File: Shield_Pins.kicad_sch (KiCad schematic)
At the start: 0 parts

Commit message: 1st push attempt
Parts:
- added AE1: Antenna, symbol Device:Antenna
- added BT1: Battery_Cell, symbol Device:Battery_Cell
- added C? (x5): C, symbol Device:C
- added L?: INDUCTOR, symbol pspice:INDUCTOR
- added P?: USB_C_Plug_USB2.0, symbol Connector:USB_C_Plug_USB2.0
- added Q?: BF244A, Package_TO_SOT_THT:TO-92_Inline, symbol Transistor_FET:BF244A
- added SW1, SW2: SW_DIP_x01, symbol Switch:SW_DIP_x01
- added U1: NEO-M8Q, RF_GPS:ublox_NEO, symbol RF_GPS:NEO-M8Q
- added U? (x2): AP2127N-3.3, Package_TO_SOT_SMD:SOT-23, symbol Regulator_Linear:AP2127N-3.3
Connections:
- new net: AE1.1 (A), C?.1, L?.1
- new net: C?.1, L?.2, SW2.1
- new net: P?.A4 (VBUS), P?.A9 (VBUS), P?.B4 (VBUS), P?.B9 (VBUS), U?.3 (VI)
- new net: BT1.2 (-), C?.2
- new net +5V: U?.3 (VI)
- new net ANT: SW2.2, U1.11 (RF_IN)
- new net BATT_3.3: BT1.1 (+), C?.1, U1.22 (V_BCKP)
- new net D_MINUS: P?.A7 (D-), U1.5 (USB_DM)
- new net D_PLUS: P?.A6 (D+), U1.6 (USB_DP)
- new net EXT_ANT_EN: U1.14 (LNA_EN)
- new net EXT_ANT_PWR: U1.9 (VCC_RF)
- new net GND: C?.2, C?.2, C?.2, C?.2, P?.A1 (GND), P?.A12 (GND), P?.B1 (GND), P?.B12 (GND), Q?.3 (S), SW1.2, U1.10 (GND), U1.12 (GND), U1.13 (GND), U1.24 (GND), U?.1 (GND), U?.1 (GND)
- new net IO.11: U1.18 (SDA/~{SPI_CS})
- new net IO.12: U1.19 (SCL/SPI_CLK)
- new net IO.7: U1.4 (EXTINT)
- new net IO.8: Q?.2 (G)
- new net IO.RX: U1.21 (RXD/SPI_MOSI)
- new net IO.SDO: U1.20 (TXD/SPI_MISO)
- new net MAIN_3.3: C?.1, U1.23 (VCC), U?.2 (VO)
- new net SERVICE: U1.1 (~{SAFEBOOT})
- new net SPI_SEL: Q?.1 (D), SW1.1, U1.2 (D_SEL)
- new net USB_3.3: C?.1, U1.7 (VDD_USB), U?.2 (VO)
- no-connect marks 5 -> 1
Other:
- note added: "Battery USB USB 5V to 3.3V 5V to 3.3V Timepulse Attatchment D_SEL Switches Reset Buttons"
- note added: "NEO-M8Q-01A"

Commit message: Schematics V1 done, still need Pi filter numbers
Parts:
- removed C?: C, symbol Device:C
- removed Q?: BF244A, Package_TO_SOT_THT:TO-92_Inline, symbol Transistor_FET:BF244A
- added C1, C5, C7: 0.1 µF, symbol Device:C
- added D1, D2, D3: LED, symbol Device:LED
- added J1, J3, J4: Conn_01x01_Male, symbol Connector:Conn_01x01_Male
- added J2: Conn_01x02_Male, symbol Connector:Conn_01x02_Male
- added R1, R2, R3: 10k, symbol Device:R
- added R4, R5: 330, symbol Device:R
- added R6: 150, symbol Device:R
- added SW1: SW_Push, symbol Switch:SW_Push
- added U1: TXB0108DQSR, Package_SON:USON-20_2x4mm_P0.4mm, symbol Logic_LevelTranslator:TXB0108DQSR
- added U1: 74LS157, symbol 74xx:74LS157
- C2, C6: renamed from C?; value C -> 0.1 µF
- gave numbers to parts that had none: 6
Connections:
- net SPI_SEL is gone; now on net +3V3: SW1.1, U1.2 (D_SEL)
- net +5V: now also C1.1, R4.1, U1.16 (VCCB)
- net ANT: now also J3.1 (Pin_1)
- net EXT_ANT_EN: now also J2.2 (Pin_2)
- net EXT_ANT_PWR: now also J2.1 (Pin_1)
- net GND: now also BT1.2 (-), C1.2, C5.2, C7.2, D1.1 (K), D2.1 (K), D3.1 (K), R1.2, R2.1, R3.1, U1.15 (GND), U1.8 (GND); no longer SW1.2
- net IO.11: now also U1.10 (I1c); no longer U1.18 (SDA/~{SPI_CS})
- net IO.12: now also U1.13 (I1d); no longer U1.19 (SCL/SPI_CLK)
- net IO.8: now also U1.20 (B1)
- net IO.RX: now also U1.6 (I1b); no longer U1.21 (RXD/SPI_MOSI)
- net IO.SDO: now also U1.2 (I0a); no longer U1.20 (TXD/SPI_MISO)
- net SERVICE: now also J1.1 (Pin_1)
- net USB_5V: now reaches P1.A4 (VBUS), P1.A9 (VBUS), P1.B4 (VBUS), P1.B9 (VBUS), U2.3 (VI)
- net USB_5V: now also C5.1, R5.1
- net at P1.A5 (CC): now also R2.2
- net at P1.B5 (VCONN): now also R1.1
- net PULSE_3.3: now reaches U1.3 (TIMEPULSE)
- net PULSE_3.3: now also R6.1, U1.3 (A3)
- net RESET: now reaches U1.8 (~{RESET})
- net RESET: now also C7.1, SW1.2, U1.2 (A2)
- net BATT_3.3 renamed BATT_3V
- net IO.7 renamed EXT_INT
- net EXT_INT: now also J4.1 (Pin_1), U1.1 (A1)
- net MAIN_3.3 renamed +3V3
- net +3V3: now also SW1.1, U1.1 (S), U1.16 (VCC), U1.5 (VCCA), U1.6 (OE)
- new net: D3.2 (A), R5.2
- new net: D2.2 (A), R4.2
- new net: R3.2, SW1.2
- new net: D1.2 (A), R6.2
- new net IO.10: U1.18 (B3)
- new net IO.9: U1.19 (B2)
- new net IO.CSB: U1.11 (I0c)
- new net IO.SCK: U1.5 (I0b)
- new net IO.SDI: U1.14 (I0d)
- new net IO.TX: U1.3 (I1a)
- new net RX_3.3: U1.21 (RXD/SPI_MOSI), U1.7 (A5)
- new net RX_SCK: U1.14 (B5), U1.7 (Zb)
- new net SCL_3.3: U1.18 (SDA/~{SPI_CS}), U1.19 (SCL/SPI_CLK), U1.8 (A6), U1.9 (A7)
- new net SCL_CLK: U1.12 (B7), U1.12 (Zd)
- new net SDA_CSB: U1.13 (B6), U1.9 (Zc)
- new net TX_3.3: U1.20 (TXD/SPI_MISO), U1.4 (A4)
- new net TX_SDO: U1.17 (B4), U1.4 (Za)
- no-connect marks 1 -> 5
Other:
- note added: "2 to 1 Multiplexer"
- note added: "5V to 3.3V LLC - Bidirectional"
- note added: "Additional Pins"
- note added: "Backup Battery"
- note added: "Main Board 5V to 3.3V"
- note added: "Passive Antenna with Switch - Internal"
- note added: "Power and Status LEDs"
- note added: "Reset Circuit"
- note added: "UART/I2C or SPI Switch"
- note added: "USB 5V to 3.3V"
- note added: "USB C Connection"
- note removed: "Battery USB USB 5V to 3.3V 5V to 3.3V Timepulse Attatchment D_SEL Switches Reset Buttons"
- moved on the sheet: AE1, BT1, C2, C3, C4, C6, L1, P1, SW1, SW2, U1, U2

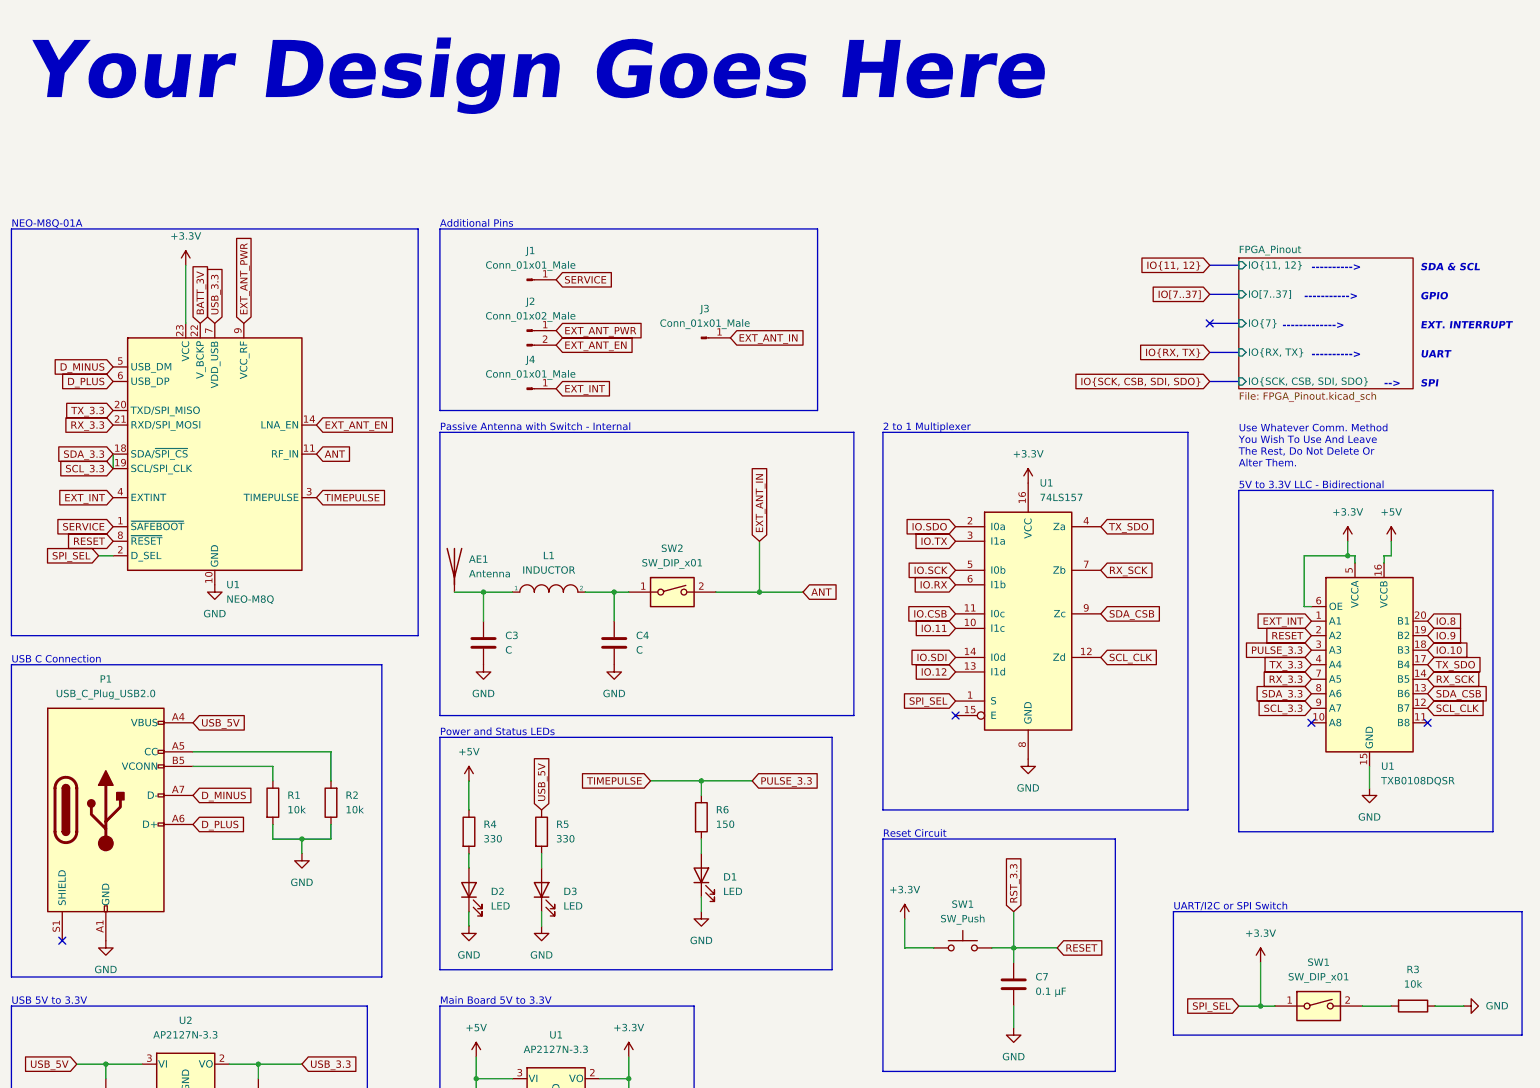
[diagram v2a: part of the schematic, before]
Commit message: Filter values added
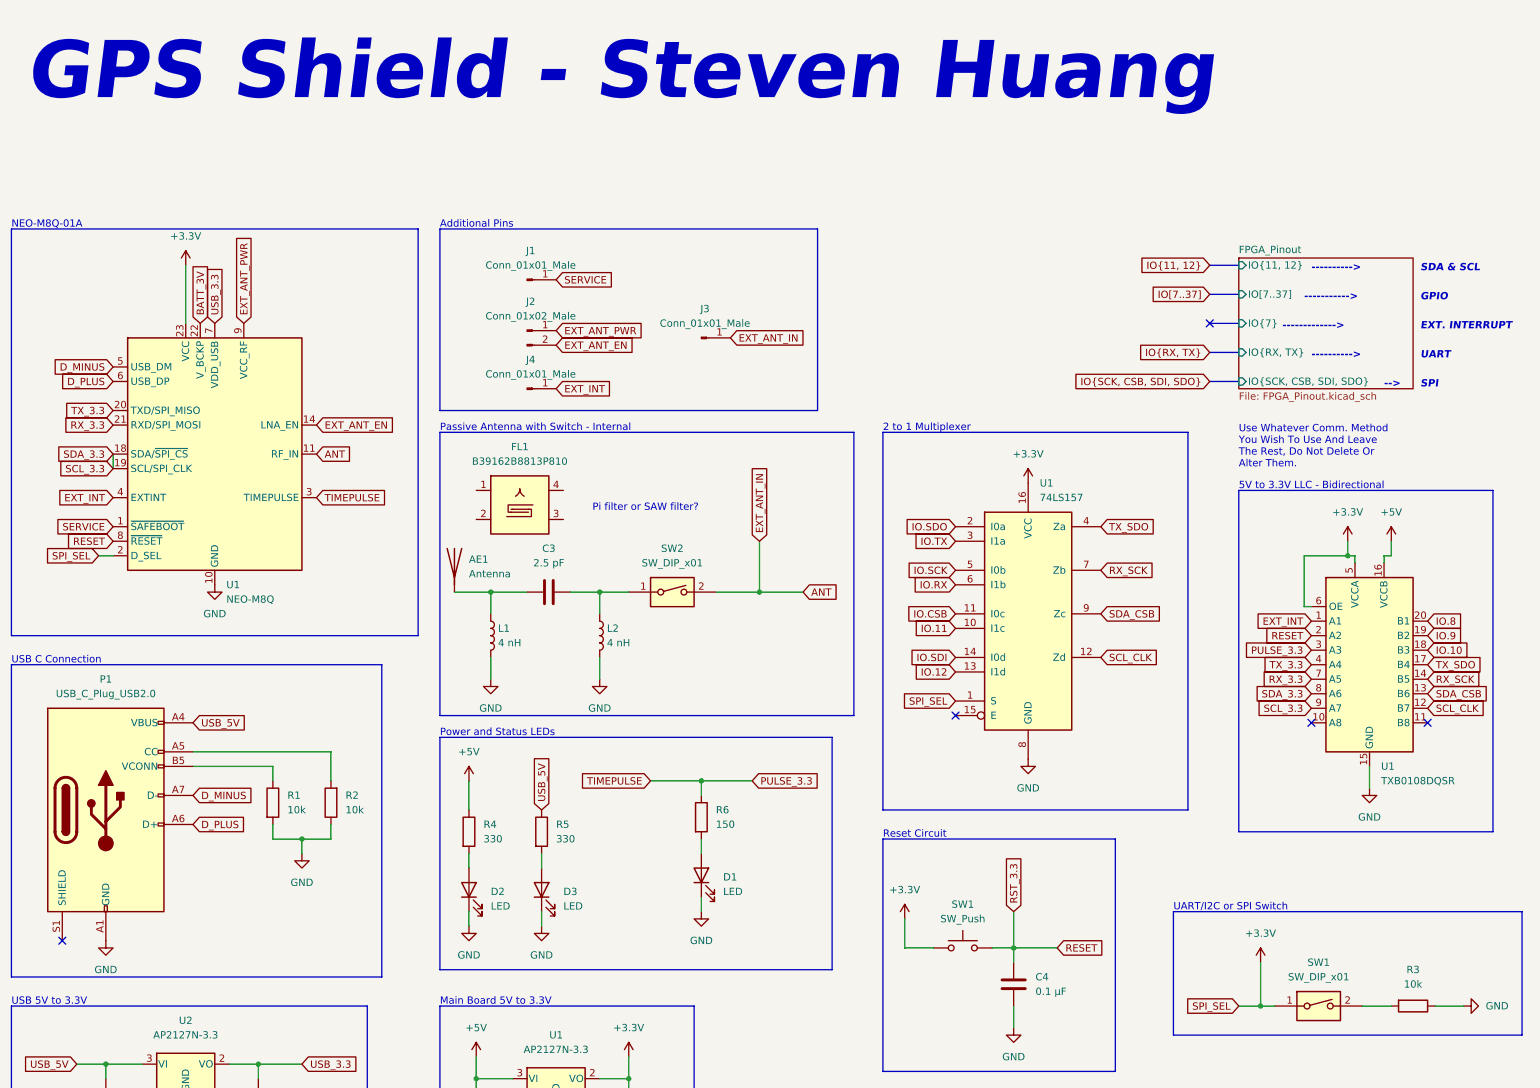
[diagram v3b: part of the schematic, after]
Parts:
- removed C4: C, symbol Device:C
- removed L1: INDUCTOR, symbol pspice:INDUCTOR
- added FL1: B39162B8813P810, Filter:Filter_1109-5_1.1x0.9mm, symbol Filter:B39162B8813P810
- added L1, L2: 4 nH, symbol Device:L
- C3: value C -> 2.5 pF
- renumbered C7 to C4
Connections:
- net GND: now also L1.2, L2.2; no longer C3.2
- net at AE1.1 (A), C3.1: now also L1.1
- net at SW2.1: now also C3.2, L2.1
- new net: FL1.2, FL1.5
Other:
- note added: "GPS Shield - Steven Huang"
- note added: "Pi filter or SAW filter?"
- note removed: "Your Design Goes Here"

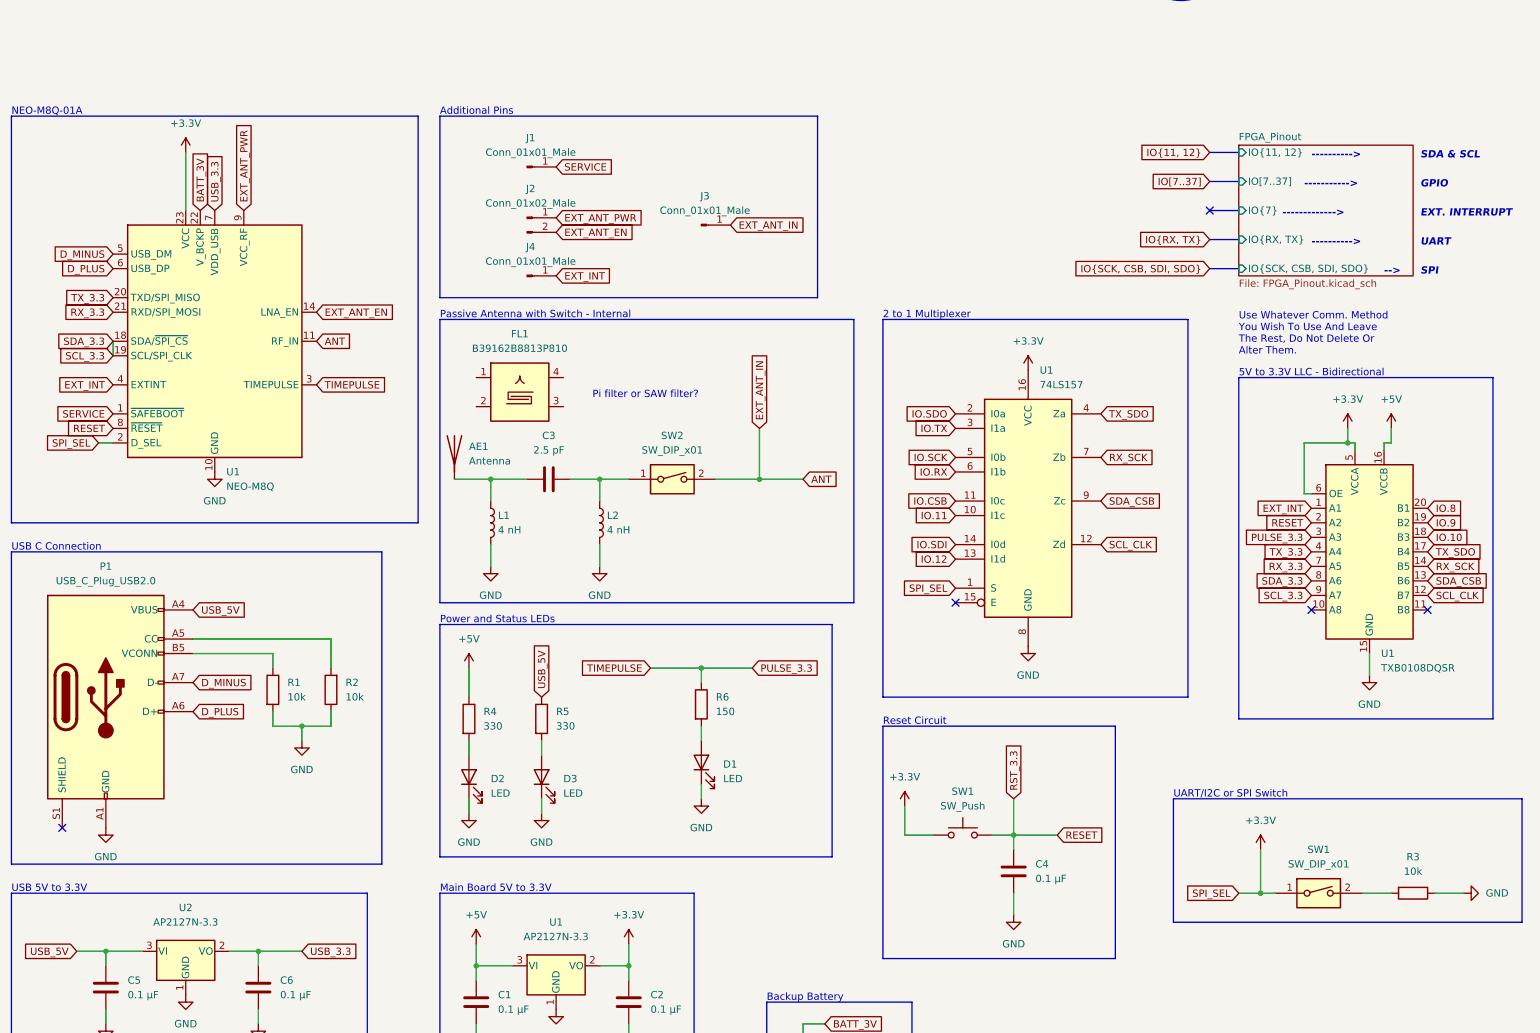
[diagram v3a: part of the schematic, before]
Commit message: fixed some erc errors and added decoupling cap
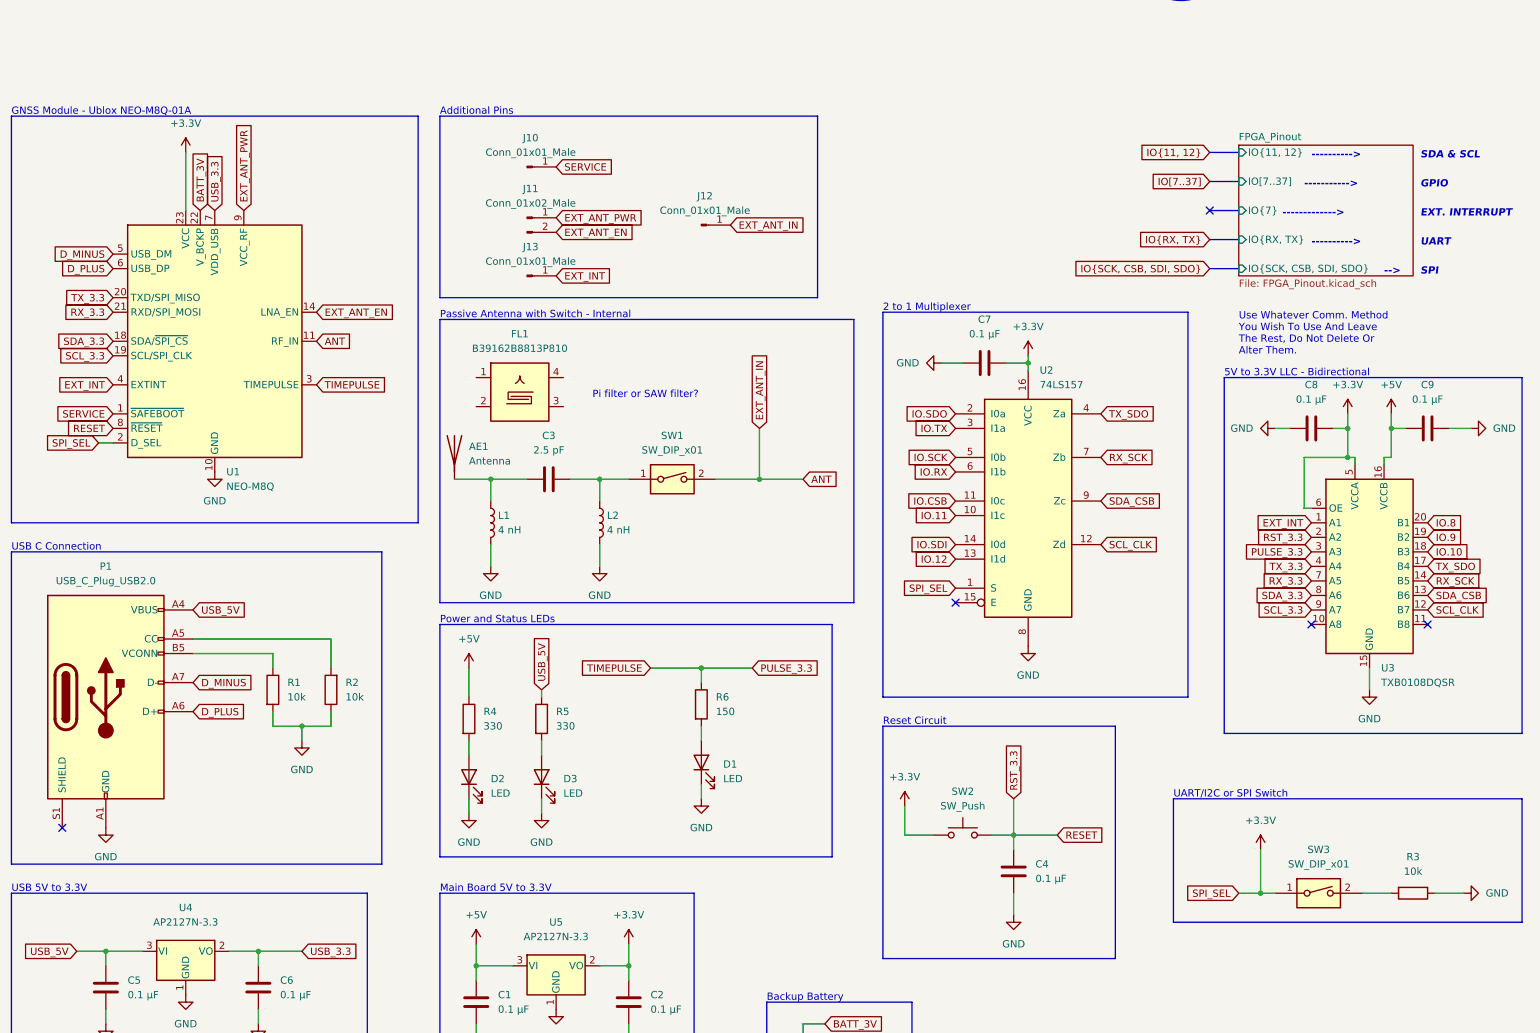
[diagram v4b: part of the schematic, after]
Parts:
- added C7, C8, C9: 0.1 µF, symbol Device:C
- renumbered J1 to J10, J2 to J11, J3 to J12, J4 to J13, SW2 to SW1, SW1 to SW2, SW1 to SW3, U1 to U2, U1 to U3, U2 to U4, U1 to U5
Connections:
- net +3V3: now also C7.2, C8.2
- net +5V: now also C9.1
- net GND: now also C7.1, C8.1, C9.2
- net SCL_3.3: no longer U1.18 (SDA/~{SPI_CS}), U3.8 (A6)
- new net SDA_3.3: U1.18 (SDA/~{SPI_CS}), U3.8 (A6)
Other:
- note added: "GNSS Module - Ublox NEO-M8Q-01A"
- note removed: "NEO-M8Q-01A"
- moved on the sheet: U3

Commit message: Day 1 feedback applied
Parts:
- removed C5, C6, C8, C9: 0.1 µF, symbol Device:C
- removed R1, R3: 10k, symbol Device:R
- removed U3: TXB0108DQSR, Package_SON:USON-20_2x4mm_P0.4mm, symbol Logic_LevelTranslator:TXB0108DQSR
- removed U4: AP2127N-3.3, Package_TO_SOT_SMD:SOT-23, symbol Regulator_Linear:AP2127N-3.3
- added C1, C2: 100n, Capacitor_SMD:C_0603_1608Metric, symbol Device:C
- added D1, D5: BAT165AX, Diode_SMD:D_0402_1005Metric, symbol Device:D_Schottky
- added FB1: 120R, Inductor_SMD:L_0603_1608Metric, symbol Device:FerriteBead
- added R5: 10k, symbol Device:R
- added R6: 11k, symbol Device:R
- added U2: AP2127N-3.3, Package_TO_SOT_SMD:SOT-23, symbol Regulator_Linear:AP2127N-3.3
- added U5: 74LVC1G18, symbol 74xGxx:74LVC1G18
- C3: value 2.5 pF -> 0.1 µF
- L1, L2: value 4 nH -> 5.1 nH
- R1: renamed from R2; value 10k -> 5.1k
- renumbered C1 to C5, C2 to C6, D1 to D4, R4 to R2, R5 to R3, R6 to R4, SW3 to SW2, SW2 to SW3, U5 to U3, U2 to U4
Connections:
- net RX_SCK is gone; now on net SDA_CSB: U4.7 (Zb)
- net SCL_3.3 is gone; now on net SCL_CLK: U1.19 (SCL/SPI_CLK)
- net SDA_3.3 is gone; now on net SDA_CSB: U1.18 (SDA/~{SPI_CS})
- net TX_SDO is gone; now on net TX_SCK: U4.4 (Za)
- net +3V3: now also D5.1 (K), R5.1, R6.2; no longer SW2.1, SW3.1, U1.2 (D_SEL), U4.1 (S)
- net GND: now also C3.2, FL1.2, FL1.3, FL1.5, SW2.2, SW3.2, U1.8 (~{RESET}), C1.2, C2.2, U2.1 (GND), U5.2 (GND)
- net IO.11: now also U4.6 (I1b); no longer U4.10 (I1c)
- net IO.12: now also U4.10 (I1c); no longer U4.13 (I1d)
- net IO.CSB: now also U4.5 (I0b); no longer U4.11 (I0c)
- net IO.RX: now also U5.4; no longer U4.6 (I1b)
- net IO.SCK: now also U4.2 (I0a); no longer U4.5 (I0b)
- net IO.SDI: now also U4.11 (I0c); no longer U4.14 (I0d)
- net IO.SDO: now also U5.6; no longer U4.2 (I0a)
- net SCL_CLK: now also U4.9 (Zc); no longer U4.12 (Zd)
- net SDA_CSB: no longer U4.9 (Zc)
- net USB_5V: now also C1.1, D1.2 (A); no longer R3.1
- net at FL1.1: now also AE1.1 (A), L1.1
- net at FL1.4: now also L2.1, SW1.1
- net PULSE_3.3 renamed TIMEPULSE
- removed net RESET: C4.1, SW3.2, U1.8 (~{RESET})
- net RX_3.3 renamed TX_SCK
- net TX_3.3 renamed RX_SDO
- net RX_SDO: now also U5.3
- net USB_3.3 renamed USB_3.3V
- net USB_3.3V: now also C4.1, D5.2 (A), U2.2 (VO)
- new net: R6.1, SW3.1
- new net: D1.1 (K), FB1.1
- new net SPI_SEL: R5.2, SW2.1, U1.2 (D_SEL), U4.1 (S), U5.1
- new net USB_Filt: C2.1, C3.1, FB1.2, R3.1, U2.3 (VI)
- new net VCC: U5.5 (VCC)
- no-connect marks 5 -> 7
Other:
- note added: "1 to 2 Demultiplexer for Transmit"
- note added: "3.3V I/O PINS ASSUMED"
- note added: "GNSS module detects board and USB power separately."
- note added: "High Pass Pi Filter is also viable. Inductors as suggested by SAW filter datasheet."
- note added: "Passive Antenna with Switch"
- note added: "USB PWR Filtering - Taken from X06"
- note removed: "5V to 3.3V LLC - Bidirectional"
- note removed: "Passive Antenna with Switch - Internal"
- note removed: "Pi filter or SAW filter?"
- moved on the sheet: AE1, BT1, C5, C6, C7, D2, D3, D4, FL1, P1, R1, R2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

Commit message: tried to fix erc errors
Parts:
- added D6: BAT165AX, Diode_SMD:D_0402_1005Metric, symbol Device:D_Schottky
- AE1: value Antenna -> W3011A
- C1, C2: value 100n -> 0.1 µF
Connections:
- net +3V3: now also D6.1 (K); no longer C6.1, U3.2 (VO)
- net IO.11 renamed IO11
- net IO.12 renamed IO12
- new net: C6.1, D6.2 (A), U3.2 (VO)
- no-connect marks 7 -> 8
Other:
- sheet FPGA_Pinout ports: added F{IO0, IO1, CLK, CSB}; removed none
